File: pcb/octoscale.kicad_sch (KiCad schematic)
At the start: 103 parts, among them J1 USB_C_Receptacle_USB2.0 TYPE-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, J2 Conn_01x04_Male, J3 Molex picoblade vertical C122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, J4 JST-SH, stemma, J5 JST-SH, J6 JST-SH, J7 Conn_01x04_Male, Q1 AO3415_C181094, Q2 MMBT44032T, Q3 S8050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

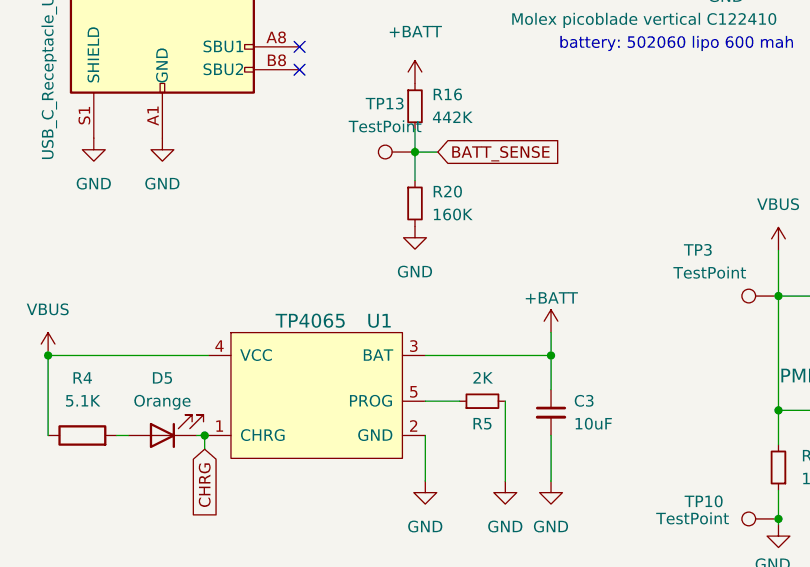
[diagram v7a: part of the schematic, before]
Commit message: Tweak charging speed
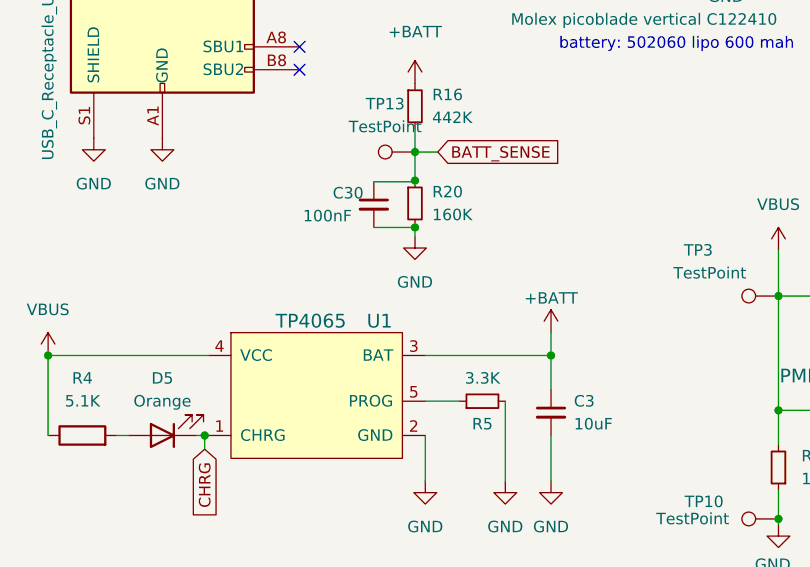
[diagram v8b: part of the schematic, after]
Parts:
- added C30: 100nF, Capacitor_SMD:C_0805_2012Metric_Pad1.18x1.45mm_HandSolder, symbol Device:C_Small
- JP2: footprint SolderJumper-2_P1.3mm_Bridged_RoundedPad1.0x1.5mm -> Jumper:SolderJumper-2_P1.3mm_Bridged_RoundedPad1.0x1.5mm
- R5: value 2K -> 3.3K
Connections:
- net BATT_SENSE: now also C30.1
- net GND: now also C30.2
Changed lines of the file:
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@@
   (junction (at 349.25 77.724) (diameter 0) (color 0 0 0 0)
   )
+  (junction (at 56.642 69.596) (diameter 0) (color 0 0 0 0)
+  )
   (junction (at 246.38 224.155) (diameter 0) (color 0 0 0 0)
   )
@@
   (junction (at 343.154 215.392) (diameter 0) (color 0 0 0 0)
   )
+  (junction (at 56.642 64.389) (diameter 0) (color 0 0 0 0)
+  )
   (junction (at 343.154 179.832) (diameter 0) (color 0 0 0 0)
   )
@@
     (stroke (width 0) (type default) (color 0 0 0 0))
   )
+  (wire (pts (xy 52.07 69.596) (xy 56.642 69.596))
+    (stroke (width 0) (type default) (color 0 0 0 0))
+  )
   (wire (pts (xy 204.47 68.834) (xy 196.85 68.834))
     (stroke (width 0) (type default) (color 0 0 0 0))
@@
     (stroke (width 0) (type default) (color 0 0 0 0))
   )
+  (wire (pts (xy 52.07 64.516) (xy 56.642 64.516))
+    (stroke (width 0) (type default) (color 0 0 0 0))
+  )
   (wire (pts (xy 65.405 272.415) (xy 80.645 272.415))
     (stroke (width 0) (type default) (color 0 0 0 0))
@@
     (stroke (width 0) (type default) (color 0 0 0 0))
   )
+  (wire (pts (xy 56.642 69.596) (xy 56.642 69.469))
+    (stroke (width 0) (type default) (color 0 0 0 0))
+  )
   (wire (pts (xy 252.73 56.134) (xy 252.73 66.294))
     (stroke (width 0) (type default) (color 0 0 0 0))
@@
     (stroke (width 0) (type default) (color 0 0 0 0))
   )
+  (wire (pts (xy 56.642 70.612) (xy 56.642 69.596))
+    (stroke (width 0) (type default) (color 0 0 0 0))
+  )
   (wire (pts (xy 196.85 71.374) (xy 200.66 71.374))
     (stroke (width 0) (type default) (color 0 0 0 0))
@@
     (stroke (width 0) (type default) (color 0 0 0 0))
   )
+  (wire (pts (xy 56.642 64.389) (xy 56.642 64.516))
+    (stroke (width 0) (type default) (color 0 0 0 0))
+  )
   (wire (pts (xy 179.07 168.91) (xy 177.8 168.91))
     (stroke (width 0) (type default) (color 0 0 0 0))
@@
     (pin "2")
   )
-  (symbol (lib_id "power:GND") (at 56.642 69.469 0) (unit 1)
+  (symbol (lib_id "power:GND") (at 56.642 70.612 0) (unit 1)
     (in_bom yes) (on_board yes) (fields_autoplaced)
-    (property "Reference" "#PWR057" (id 0) (at 56.642 75.819 0)
+    (property "Reference" "#PWR057" (id 0) (at 56.642 76.962 0)
       (effects (font (size 1.27 1.27)) hide)
     )
-    (property "Value" "GND" (id 1) (at 56.642 74.549 0))
-    (property "Footprint" "" (id 2) (at 56.642 69.469 0)
+    (property "Value" "GND" (id 1) (at 56.642 75.692 0))
+    (property "Footprint" "" (id 2) (at 56.642 70.612 0)
       (effects (font (size 1.27 1.27)) hide)
     )
-    (property "Datasheet" "" (id 3) (at 56.642 69.469 0)
+    (property "Datasheet" "" (id 3) (at 56.642 70.612 0)
       (effects (font (size 1.27 1.27)) hide)
     )
@@
     (in_bom yes) (on_board yes)
     (property "Reference" "R5" (id 0) (at 64.135 91.44 90))
-    (property "Value" "2K" (id 1) (at 64.135 86.36 90))
+    (property "Value" "3.3K" (id 1) (at 64.135 86.36 90))
     (property "Footprint" "Resistor_SMD:R_0805_2012Metric_Pad1.20x1.40mm_HandSolder" (id 2) (at 64.135 88.9 0)
       (effects (font (size 1.27 1.27)) hide)
@@
     (pin "1")
   )
+  (symbol (lib_id "Device:C_Small") (at 52.07 67.056 0) (unit 1)
+    (in_bom yes) (on_board yes)
+    (property "Reference" "C30" (id 0) (at 47.498 65.786 0)
+      (effects (font (size 1.27 1.27)) (justify left))
+    )
+    (property "Value" "100nF" (id 1) (at 44.196 68.326 0)
+      (effects (font (size 1.27 1.27)) (justify left))
+    )
+    (property "Footprint" "Capacitor_SMD:C_0805_2012Metric_Pad1.18x1.45mm_HandSolder" (id 2) (at 52.07 67.056 0)
+      (effects (font (size 1.27 1.27)) hide)
+    )
+    (property "Datasheet" "~" (id 3) (at 52.07 67.056 0)
+      (effects (font (size 1.27 1.27)) hide)
+    )
+    (pin "1")
+    (pin "2")
+  )
   (symbol (lib_id "power:GND") (at 208.28 67.564 0) (unit 1)
     (in_bom yes) (on_board yes) (fields_autoplaced)
@@
       (effects (font (size 1.27 1.27)) (justify right))
     )
-    (property "Footprint" "SolderJumper-2_P1.3mm_Bridged_RoundedPad1.0x1.5mm" (id 2) (at 133.604 23.622 0)
+    (property "Footprint" "Jumper:SolderJumper-2_P1.3mm_Bridged_RoundedPad1.0x1.5mm" (id 2) (at 133.604 23.622 0)
       (effects (font (size 1.27 1.27)) hide)
     )
@@
       (reference "C29") (unit 1) (value "1uF") (footprint "Capacitor_SMD:C_0805_2012Metric_Pad1.18x1.45mm_HandSolder")
     )
+    (path "/c043ba1a-7796-495c-bc6f-bbc64562a09d"
+      (reference "C30") (unit 1) (value "100nF") (footprint "Capacitor_SMD:C_0805_2012Metric_Pad1.18x1.45mm_HandSolder")
+    )
     (path "/ef400044-7c2a-4df6-9fdd-73ebbc085c73"
       (reference "D1") (unit 1) (value "WS2812B-2020") (footprint "easyeda2kicad:LED-SMD_4P-L2.0-W2.0-TL_WS2812B-2020")
@@
     )
     (path "/fd6e8f97-3626-420e-8c24-4a9a91138c41"
-      (reference "JP2") (unit 1) (value "SolderJumper_2_Bridged") (footprint "SolderJumper-2_P1.3mm_Bridged_RoundedPad1.0x1.5mm")
+      (reference "JP2") (unit 1) (value "SolderJumper_2_Bridged") (footprint "Jumper:SolderJumper-2_P1.3mm_Bridged_RoundedPad1.0x1.5mm")
     )
     (path "/055e53a3-5962-4f31-92ff-64f5300dbf30"
@@
     )
     (path "/afe3a168-53c2-403b-85c4-9ab0258dc168"
-      (reference "R5") (unit 1) (value "2K") (footprint "Resistor_SMD:R_0805_2012Metric_Pad1.20x1.40mm_HandSolder")
+      (reference "R5") (unit 1) (value "3.3K") (footprint "Resistor_SMD:R_0805_2012Metric_Pad1.20x1.40mm_HandSolder")
     )
     (path "/77168437-e7f0-4dc7-94fc-314d05d47182"
